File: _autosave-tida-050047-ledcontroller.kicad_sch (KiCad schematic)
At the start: 139 parts, among them Q1 AOD424, Q2 AOD424, U1 TPS25750DRJKR, U10 XT30PW-F, U11 HY2213-BB3A, U12 HY2213-BB3A, U13 AP2300-ES, U14 AP2300-ES, U15 SB1045L_C2844167, U16 BQ7790400PWR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

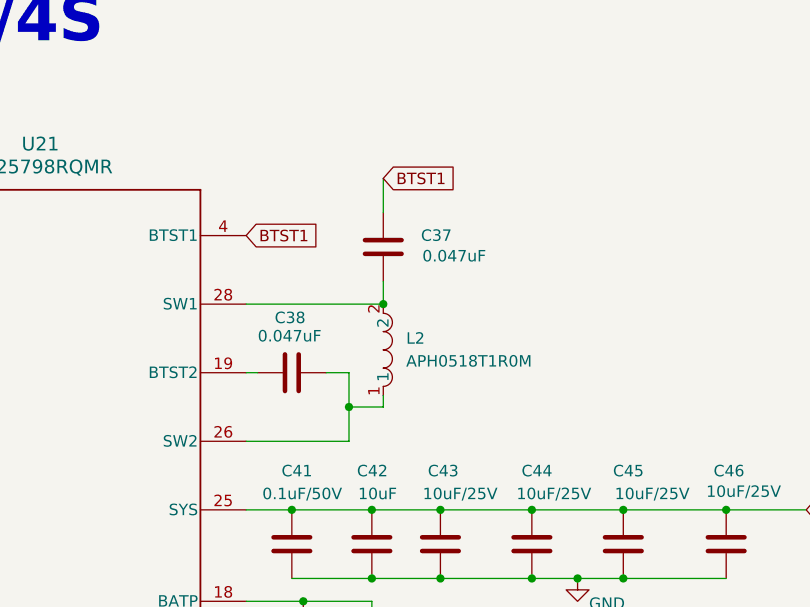
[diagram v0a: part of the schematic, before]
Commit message: update schematics, add cell monitors that switches cells off if something is wrong, started pcb layout
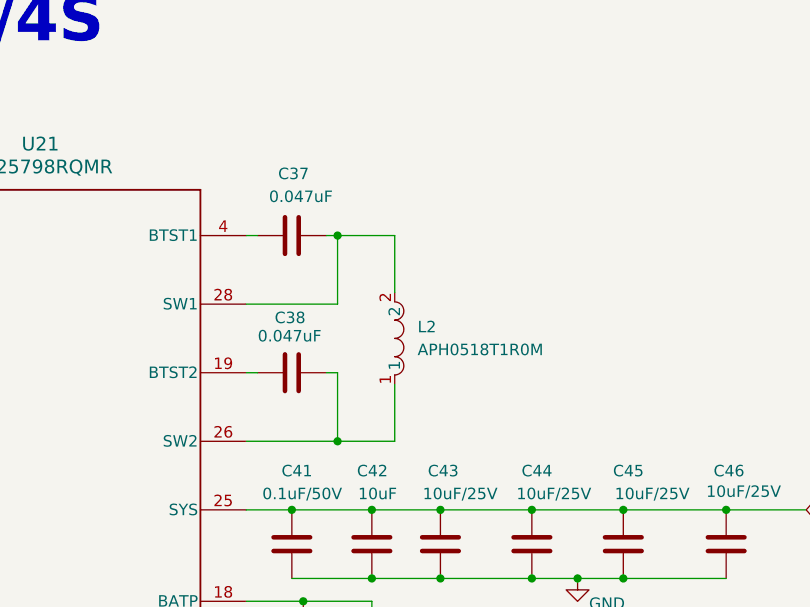
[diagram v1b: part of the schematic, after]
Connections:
- net BTST1: no longer names the net of C37.2, U21.4 (BTST1)
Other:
- moved on the sheet: L2
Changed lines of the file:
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@@
 	)
 	(junction
-		(at 359.41 151.13)
-		(diameter 0)
-		(color 0 0 0 0)
-	)
-	(junction
 		(at 386.08 173.99)
 		(diameter 0)
@@
 	)
 	(junction
+		(at 354.33 166.37)
+		(diameter 0)
+		(color 0 0 0 0)
+	)
+	(junction
 		(at 419.1 63.5)
 		(diameter 0)
@@
 	)
 	(junction
-		(at 355.6 162.56)
-		(diameter 0)
-		(color 0 0 0 0)
-	)
-	(junction
 		(at 135.89 219.71)
 		(diameter 0)
@@
 	)
 	(junction
+		(at 354.33 143.51)
+		(diameter 0)
+		(color 0 0 0 0)
+	)
+	(junction
 		(at 346.71 87.63)
 		(diameter 0)
@@
 	(wire
 		(pts
+			(xy 354.33 151.13) (xy 354.33 143.51)
+		)
+		(stroke
+			(width 0)
+			(type default)
+		)
+	)
+	(wire
+		(pts
+			(xy 353.06 143.51) (xy 354.33 143.51)
+		)
+		(stroke
+			(width 0)
+			(type default)
+		)
+	)
+	(wire
+		(pts
 			(xy 265.43 143.51) (xy 273.05 143.51)
 		)
@@
 	(wire
 		(pts
+			(xy 354.33 166.37) (xy 360.68 166.37)
+		)
+		(stroke
+			(width 0)
+			(type default)
+		)
+	)
+	(wire
+		(pts
 			(xy 735.33 312.42) (xy 735.33 318.77)
 		)
@@
 	(wire
 		(pts
-			(xy 355.6 158.75) (xy 355.6 162.56)
+			(xy 354.33 158.75) (xy 354.33 166.37)
 		)
 		(stroke
@@
 	(wire
 		(pts
-			(xy 359.41 148.59) (xy 359.41 151.13)
-		)
-		(stroke
-			(width 0)
-			(type default)
-		)
-	)
-	(wire
-		(pts
 			(xy 120.65 252.73) (xy 139.7 252.73)
 		)
@@
 	(wire
 		(pts
-			(xy 359.41 162.56) (xy 359.41 161.29)
+			(xy 360.68 166.37) (xy 360.68 160.02)
 		)
 		(stroke
@@
 	(wire
 		(pts
-			(xy 359.41 137.16) (xy 359.41 140.97)
-		)
-		(stroke
-			(width 0)
-			(type default)
-		)
-	)
-	(wire
-		(pts
 			(xy 834.39 267.97) (xy 836.93 267.97)
 		)
@@
 	(wire
 		(pts
+			(xy 345.44 143.51) (xy 344.17 143.51)
+		)
+		(stroke
+			(width 0)
+			(type default)
+		)
+	)
+	(wire
+		(pts
 			(xy 44.45 135.89) (xy 60.96 135.89)
 		)
@@
 	(wire
 		(pts
+			(xy 360.68 143.51) (xy 360.68 149.86)
+		)
+		(stroke
+			(width 0)
+			(type default)
+		)
+	)
+	(wire
+		(pts
 			(xy 392.43 332.74) (xy 342.9 332.74)
 		)
@@
 	(wire
 		(pts
-			(xy 353.06 158.75) (xy 355.6 158.75)
+			(xy 353.06 158.75) (xy 354.33 158.75)
 		)
 		(stroke
@@
 	(wire
 		(pts
-			(xy 355.6 166.37) (xy 355.6 162.56)
-		)
-		(stroke
-			(width 0)
-			(type default)
-		)
-	)
-	(wire
-		(pts
 			(xy 386.08 181.61) (xy 381 181.61)
 		)
@@
 	(wire
 		(pts
+			(xy 344.17 151.13) (xy 354.33 151.13)
+		)
+		(stroke
+			(width 0)
+			(type default)
+		)
+	)
+	(wire
+		(pts
 			(xy 445.77 306.07) (xy 449.58 306.07)
 		)
@@
 	(wire
 		(pts
-			(xy 344.17 166.37) (xy 355.6 166.37)
+			(xy 344.17 166.37) (xy 354.33 166.37)
 		)
 		(stroke
@@
 	(wire
 		(pts
-			(xy 359.41 151.13) (xy 344.17 151.13)
-		)
-		(stroke
-			(width 0)
-			(type default)
-		)
-	)
-	(wire
-		(pts
 			(xy 44.45 106.68) (xy 45.72 106.68)
 		)
@@
 	(wire
 		(pts
-			(xy 359.41 162.56) (xy 355.6 162.56)
-		)
-		(stroke
-			(width 0)
-			(type default)
-		)
-	)
-	(wire
-		(pts
 			(xy 345.44 201.93) (xy 344.17 201.93)
 		)
@@
 	(wire
 		(pts
+			(xy 354.33 143.51) (xy 360.68 143.51)
+		)
+		(stroke
+			(width 0)
+			(type default)
+		)
+	)
+	(wire
+		(pts
 			(xy 279.4 135.89) (xy 285.75 135.89)
 		)
@@
 		)
 	)
-	(global_label "BTST1"
-		(shape input)
-		(at 359.41 137.16 0)
-		(fields_autoplaced yes)
-		(effects
-			(font
-				(size 1.27 1.27)
-			)
-			(justify left)
-		)
-		(property "Intersheetrefs" "${INTERSHEET_REFS}"
-			(at 368.0194 137.16 0)
-			(effects
-				(font
-					(size 1.27 1.27)
-				)
-				(justify left)
-				(hide yes)
-			)
-		)
-	)
 	(global_label "I2C1_SCL"
 		(shape input)
@@
 		)
 	)
-	(global_label "BTST1"
-		(shape input)
-		(at 344.17 143.51 0)
-		(fields_autoplaced yes)
-		(effects
-			(font
-				(size 1.27 1.27)
-			)
-			(justify left)
-		)
-		(property "Intersheetrefs" "${INTERSHEET_REFS}"
-			(at 352.7794 143.51 0)
-			(effects
-				(font
-					(size 1.27 1.27)
-				)
-				(justify left)
-				(hide yes)
-			)
-		)
-	)
 	(global_label "LDO_3V3"
 		(shape input)
@@
 	(symbol
 		(lib_id "easyeda2kicad:APH0518T1R0M")
-		(at 359.41 156.21 270)
+		(at 360.68 154.94 270)
 		(unit 1)
 		(exclude_from_sim no)
@@
 		(fields_autoplaced yes)
 		(property "Reference" "L2"
-			(at 361.95 154.9399 90)
+			(at 363.22 153.6699 90)
 			(effects
 				(font
@@
 		)
 		(property "Value" "APH0518T1R0M"
-			(at 361.95 157.4799 90)
+			(at 363.22 156.2099 90)
 			(effects
 				(font
@@
 		)
 		(property "Footprint" "easyeda2kicad:IND-SMD_L5.4-W5.2"
-			(at 351.79 156.21 0)
+			(at 353.06 154.94 0)
 			(effects
 				(font
@@
 		)
 		(property "Datasheet" ""
-			(at 359.41 156.21 0)
+			(at 360.68 154.94 0)
 			(effects
 				(font
@@
 		)
 		(property "Description" ""
-			(at 359.41 156.21 0)
+			(at 360.68 154.94 0)
 			(effects
 				(font
@@
 		)
 		(property "LCSC Part" "C5349672"
-			(at 349.25 156.21 0)
+			(at 350.52 154.94 0)
 			(effects
 				(font
@@
 	)
 	(symbol
-		(lib_id "Device:C")
-		(at 359.41 144.78 180)
-		(unit 1)
-		(exclude_from_sim no)
-		(in_bom yes)
-		(on_board yes)
-		(dnp no)
-		(property "Reference" "C37"
-			(at 367.03 143.51 0)
-			(effects
-				(font
-					(size 1.27 1.27)
-				)
-				(justify left)
-			)
-		)
-		(property "Value" "0.047uF"
-			(at 370.84 145.796 0)
-			(effects
-				(font
-					(size 1.27 1.27)
-				)
-				(justify left)
-			)
-		)
-		(property "Footprint" "Capacitor_SMD:C_0603_1608Metric_Pad1.08x0.95mm_HandSolder"
-			(at 358.4448 140.97 0)
-			(effects
-				(font
-					(size 1.27 1.27)
-				)
-				(hide yes)
-			)
-		)
-		(property "Datasheet" "~"
-			(at 359.41 144.78 0)
-			(effects
-				(font
-					(size 1.27 1.27)
-				)
-				(hide yes)
-			)
-		)
-		(property "Description" ""
-			(at 359.41 144.78 0)
-			(effects
-				(font
-					(size 1.27 1.27)
-				)
-				(hide yes)
-			)
-		)
-		(pin "1"
-		)
-		(pin "2"
-		)
-		(instances
-			(project "tida-050047-ledcontroller"
-				(path "/1e670a1b-cbb1-4da3-a64e-ffa1c686d3c7"
-					(reference "C37")
-					(unit 1)
-				)
-			)
-		)
-	)
-	(symbol
 		(lib_id "Device:R")
 		(at 113.03 158.75 0)
@@
 					(unit 1)
 				)
+			)
+		)
+	)
+	(symbol
+		(lib_id "Device:C")
+		(at 349.25 143.51 270)
+		(unit 1)
+		(exclude_from_sim no)
+		(in_bom yes)
+		(on_board yes)
+		(dnp no)
+		(property "Reference" "C37"
+			(at 347.726 136.652 90)
+			(effects
+				(font
+					(size 1.27 1.27)
+				)
+				(justify left)
+			)
+		)
+		(property "Value" "0.047uF"
+			(at 346.71 139.192 90)
+			(effects
+				(font
+					(size 1.27 1.27)
+				)
+				(justify left)
+			)
+		)
+		(property "Footprint" "Capacitor_SMD:C_0603_1608Metric_Pad1.08x0.95mm_HandSolder"
+			(at 345.44 144.4752 0)
+			(effects
+				(font
+					(size 1.27 1.27)
+				)
+				(hide yes)
+			)
+		)
+		(property "Datasheet" "~"
+			(at 349.25 143.51 0)
+			(effects
+				(font
+					(size 1.27 1.27)
+				)
+				(hide yes)
+			)
+		)
+		(property "Description" ""
+			(at 349.25 143.51 0)
+			(effects
+				(font
+					(size 1.27 1.27)
+				)
+				(hide yes)
+			)
+		)
+		(pin "1"
+		)
+		(pin "2"
+		)
+		(instances
+			(project "tida-050047-ledcontroller"
+				(path "/1e670a1b-cbb1-4da3-a64e-ffa1c686d3c7"
+					(reference "C37")
+					(unit 1)
+				)
